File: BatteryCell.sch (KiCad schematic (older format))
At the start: 10 parts

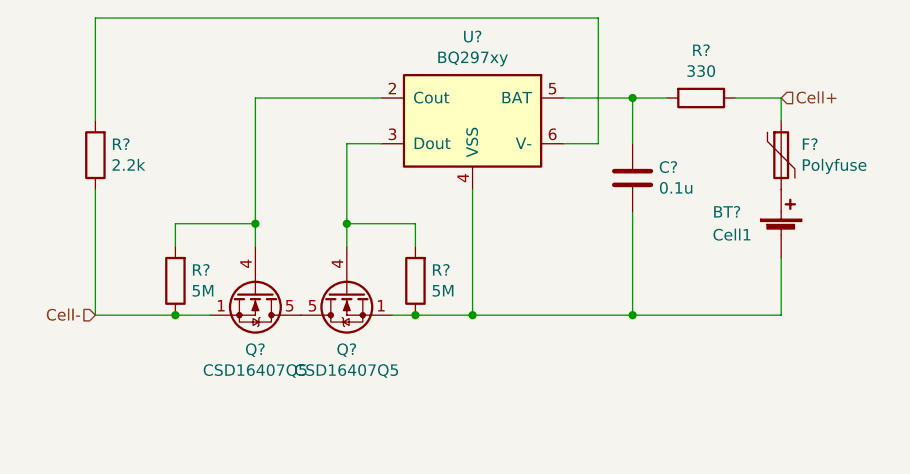
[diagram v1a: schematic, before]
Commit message: updated MOSFET model in battery cell protection schematic. Refused PTC fuse due to uncertain behaviour under conformal coating and in vacuum.
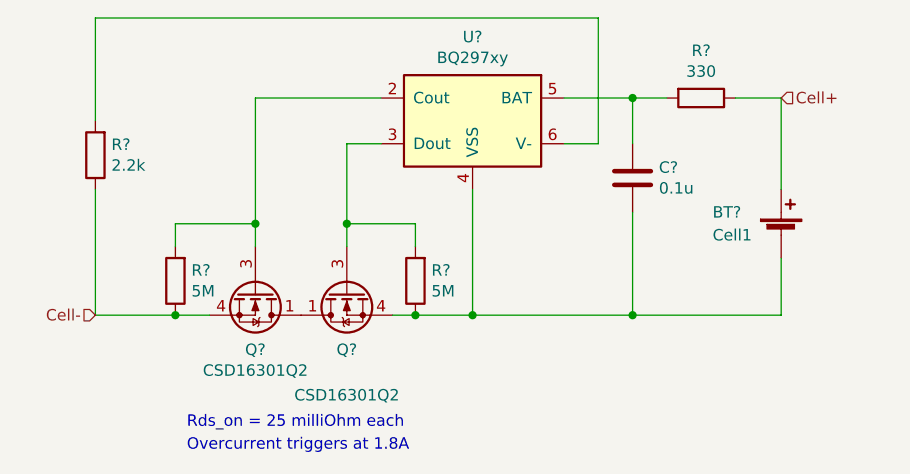
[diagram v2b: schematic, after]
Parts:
- removed F?: Polyfuse, symbol Device:Polyfuse
- removed Q? (x2): CSD16407Q5, Package_TO_SOT_SMD:TDSON-8-1, symbol Transistor_FET:CSD16407Q5
- added Q? (x2): CSD16301Q2, Package_SON:Texas_DQK, symbol Transistor_FET:CSD16301Q2
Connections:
- net Cell+: now also BT?.1 (+)
- net Cell-: now also Q?.4 (S), Q?.7 (S)
- net at BT?.2 (-), C?.2, R?.1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: now also Q?.4 (S), Q?.7 (S)
- net at R?.2, U?.3 (Dout): now also Q?.3 (G)
- net at R?.2, U?.2 (Cout): now also Q?.3 (G)
- new net: Q?.1 (D), Q?.1 (D), Q?.2 (D), Q?.2 (D), Q?.5 (D), Q?.5 (D), Q?.6 (D), Q?.6 (D), Q?.8 (D), Q?.8 (D)
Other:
- note added: "Overcurrent triggers at 1.8A"
- note added: "Rds_on = 25 milliOhm each"
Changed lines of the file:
@@
 $Descr A4 11693 8268
 encoding utf-8
-Sheet 31 34
+Sheet 27 34
 Title ""
 Date ""
@@
 $EndComp
 $Comp
-L Device:Polyfuse F?
-U 1 1 5D087B42
-P 7050 3750
-AR Path="/5D087B42" Ref="F?"  Part="1"
-AR Path="/5D07F3FC/5D087B42" Ref="F?"  Part="1"
-AR Path="/5D0A75A0/5D087B42" Ref="F?"  Part="1"
-AR Path="/5D0B1FBC/5D087B42" Ref="F?"  Part="1"
-AR Path="/5D0BC9BA/5D087B42" Ref="F?"  Part="1"
-F 0 "F?" H 7138 3796 50  0000 L CNN
-F 1 "Polyfuse" H 7138 3705 50  0000 L CNN
-F 2 "" H 7100 3550 50  0001 L CNN
-F 3 "~" H 7050 3750 50  0001 C CNN
-	1    7050 3750
-	1    0    0    -1
-$EndComp
-$Comp
 L Battery_Management:BQ297xy U?
 U 1 1 5D087B48
@@
 	-1   0    0    -1
 $EndComp
-$Comp
-L Transistor_FET:CSD16407Q5 Q?
-U 1 1 5D087B4E
-P 4750 4350
-AR Path="/5D087B4E" Ref="Q?"  Part="1"
-AR Path="/5D07F3FC/5D087B4E" Ref="Q?"  Part="1"
-AR Path="/5D0A75A0/5D087B4E" Ref="Q?"  Part="1"
-AR Path="/5D0B1FBC/5D087B4E" Ref="Q?"  Part="1"
-AR Path="/5D0BC9BA/5D087B4E" Ref="Q?"  Part="1"
-F 0 "Q?" V 5001 4350 50  0000 C CNN
-F 1 "CSD16407Q5" V 5092 4350 50  0000 C CNN
-F 2 "Package_TO_SOT_SMD:TDSON-8-1" H 4950 4275 50  0001 L CIN
-F 3 "http://www.ti.com/lit/gpn/csd16407q5" V 4750 4350 50  0001 L CNN
-	1    4750 4350
-	0    1    1    0
-$EndComp
-$Comp
-L Transistor_FET:CSD16407Q5 Q?
-U 1 1 5D087B54
-P 5150 4350
-AR Path="/5D087B54" Ref="Q?"  Part="1"
-AR Path="/5D07F3FC/5D087B54" Ref="Q?"  Part="1"
-AR Path="/5D0A75A0/5D087B54" Ref="Q?"  Part="1"
-AR Path="/5D0B1FBC/5D087B54" Ref="Q?"  Part="1"
-AR Path="/5D0BC9BA/5D087B54" Ref="Q?"  Part="1"
-F 0 "Q?" V 5401 4350 50  0000 C CNN
-F 1 "CSD16407Q5" V 5492 4350 50  0000 C CNN
-F 2 "Package_TO_SOT_SMD:TDSON-8-1" H 5350 4275 50  0001 L CIN
-F 3 "http://www.ti.com/lit/gpn/csd16407q5" V 5150 4350 50  0001 L CNN
-	1    5150 4350
-	0    -1   1    0
-$EndComp
 Wire Wire Line
 	5300 3700 5150 3700
@@
 Wire Wire Line
 	6850 3500 7050 3500
-Wire Wire Line
-	7050 3500 7050 3600
 $Comp
 L Device:C C?
@@
 Wire Wire Line
 	4050 3150 6250 3150
-Connection ~ 5450 4450
-Wire Wire Line
-	5450 4450 5350 4450
 Connection ~ 4400 4450
 Wire Wire Line
@@
 Wire Wire Line
 	5150 4050 5150 4150
+Text Notes 4450 4950 0    50   ~ 0
+Rds_on = 25 milliOhm each
+Text Notes 4450 5050 0    50   ~ 0
+Overcurrent triggers at 1.8A
+$Comp
+L Transistor_FET:CSD16301Q2 Q?
+U 1 1 5D0458C0
+P 4750 4350
+F 0 "Q?" V 5001 4350 50  0000 C CNN
+F 1 "CSD16301Q2" V 5092 4350 50  0000 C CNN
+F 2 "Package_SON:Texas_DQK" H 4950 4275 50  0001 L CIN
+F 3 "http://www.ti.com/lit/ds/symlink/csd16301q2.pdf" V 4750 4350 50  0001 L CNN
+	1    4750 4350
+	0    1    1    0
+$EndComp
+Connection ~ 5450 4450
+$Comp
+L Transistor_FET:CSD16301Q2 Q?
+U 1 1 5D04731F
+P 5150 4350
+F 0 "Q?" V 5401 4350 50  0000 C CNN
+F 1 "CSD16301Q2" V 5600 4350 50  0000 C CNN
+F 2 "Package_SON:Texas_DQK" H 5350 4275 50  0001 L CIN
+F 3 "http://www.ti.com/lit/ds/symlink/csd16301q2.pdf" V 5150 4350 50  0001 L CNN
+	1    5150 4350
+	0    -1   1    0
+$EndComp
+Wire Wire Line
+	5450 4450 5350 4450
+Wire Wire Line
+	7050 3500 7050 3900
 $EndSCHEMATC
